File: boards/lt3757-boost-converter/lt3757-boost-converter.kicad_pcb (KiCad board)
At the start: 2 copper layers, 43.8 x 64.8 mm, 40 parts, among them J1 GND, J2 Enable, J3 BAT, J4 24V, J5 M3, J6 M3, J7 M3, J8 M3, J9 GND, Q1 FDB86566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

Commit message: [lt3757-boost-converter] add rev3 to silkscreen, set page properties
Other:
- board text added: "rev3"
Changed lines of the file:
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@@
     (links 69)
     (no_connects 1)
-    (area 46.914999 27.229999 90.880001 92.150001)
+    (area 46.355 22.13 92.184 94.175)
     (thickness 1.6)
-    (drawings 30)
+    (drawings 31)
     (tracks 120)
     (zones 0)
@@
     (nets 19)
   )
-  (page A4)
+  (page User 200 150.012)
+  (title_block
+    (title "24V Boost Converter")
+    (date 2017-06-19)
+    (rev rev3)
+    (company VIPER)
+  )
   (layers
     (0 F.Cu signal)
@@
       (net 2 GND))
   )
+  (gr_text rev3 (at 67.945 31.115 270) (layer F.SilkS)
+    (effects (font (size 1.5 1.5) (thickness 0.3)))
+  )
   (gr_line (start 46.99 34.29) (end 53.975 34.29) (layer F.SilkS) (width 0.2))

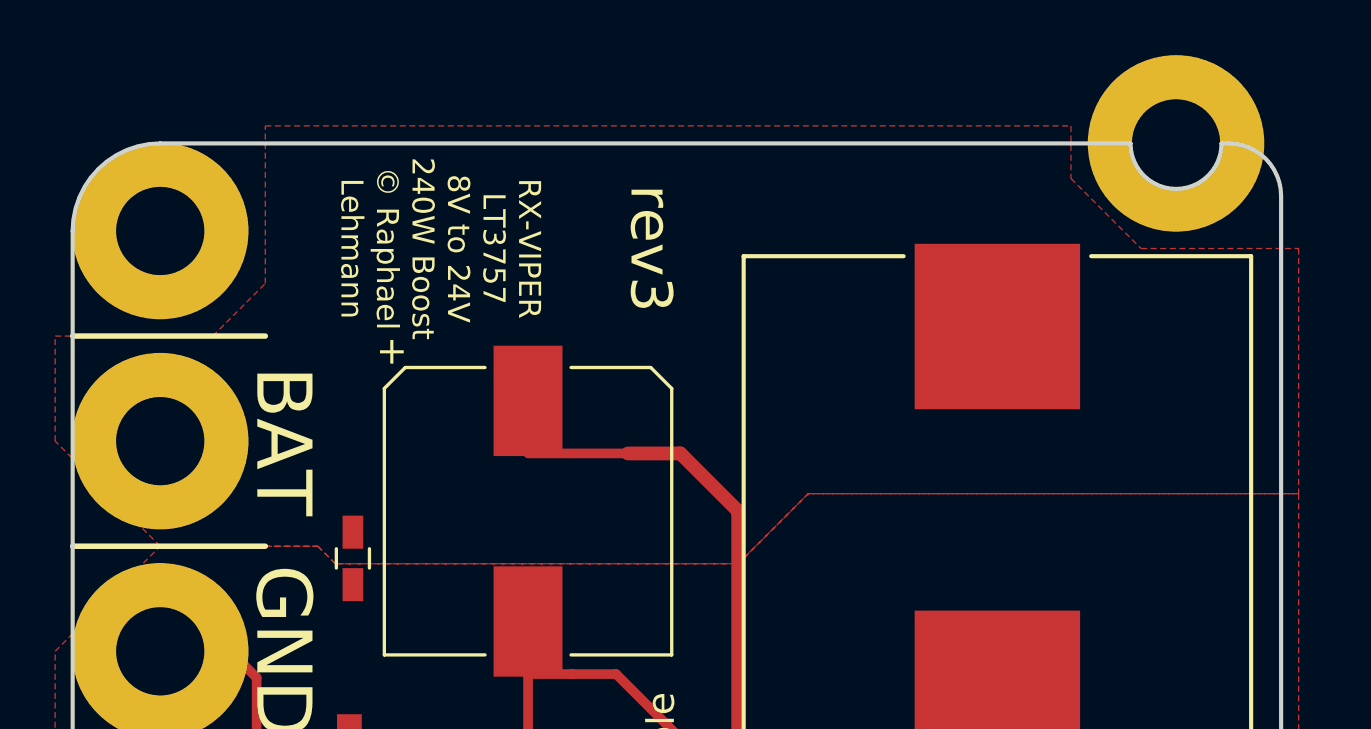
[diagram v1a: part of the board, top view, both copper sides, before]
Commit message: [lt3757-boost-converter] add label to cu layer
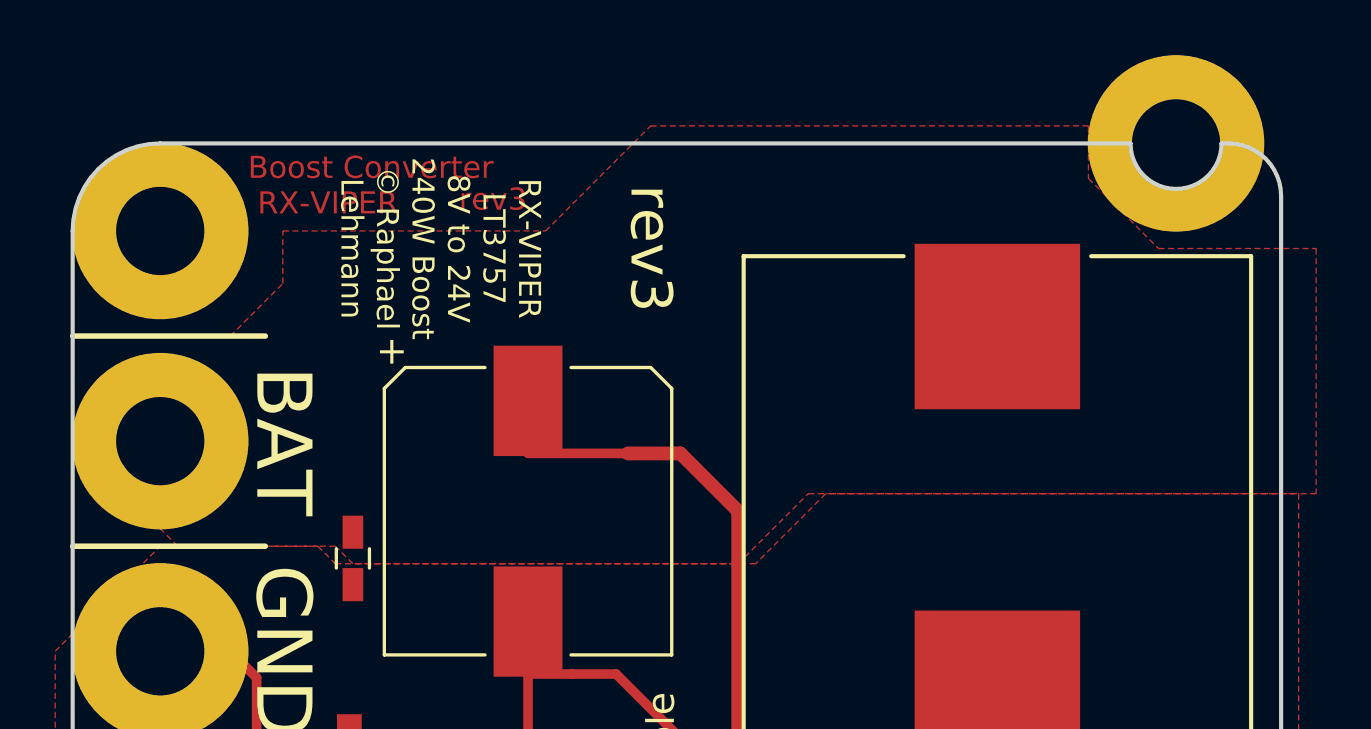
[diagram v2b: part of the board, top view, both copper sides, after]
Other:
- board text added: "Boost Converter RX-VIPER"
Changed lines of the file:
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@@
     (links 69)
     (no_connects 1)
-    (area 46.355 22.13 92.184 94.175)
+    (area 46.914999 27.229999 90.880001 92.150001)
     (thickness 1.6)
-    (drawings 31)
+    (drawings 33)
     (tracks 120)
     (zones 0)
@@
     (35 F.Paste user)
     (36 B.SilkS user)
-    (37 F.SilkS user)
+    (37 F.SilkS user hide)
     (38 B.Mask user)
     (39 F.Mask user)
@@
     (visible_elements FFFFFF7F)
     (pcbplotparams
-      (layerselection 0x00030_80000001)
-      (usegerberextensions false)
+      (layerselection 0x01080_00000001)
+      (usegerberextensions true)
       (excludeedgelayer true)
       (linewidth 0.100000)
       (plotframeref false)
-      (viasonmask false)
+      (viasonmask true)
       (mode 1)
       (useauxorigin false)
@@
       (outputformat 1)
       (mirror false)
-      (drillshape 1)
+      (drillshape 0)
       (scaleselection 1)
-      (outputdirectory ""))
+      (outputdirectory gerber/))
   )
   (net 0 "")
@@
     (pad 1 thru_hole circle (at 0 0) (size 6.4 6.4) (drill 3.2) (layers *.Cu *.Mask)
       (net 2 GND))
+  )
+  (gr_text rev3 (at 62.23 29.337) (layer F.Cu)
+    (effects (font (size 0.8 0.8) (thickness 0.15)))
+  )
+  (gr_text "Boost Converter\n RX-VIPER" (at 53.34 28.829) (layer F.Cu)
+    (effects (font (size 0.8 0.8) (thickness 0.15)) (justify left))
   )
   (gr_text rev3 (at 67.945 31.115 270) (layer F.SilkS)
@@
     (polygon
       (pts
-        (xy 53.975 32.385) (xy 53.975 26.67) (xy 83.185 26.67) (xy 83.185 28.575) (xy 85.725 31.115)
-        (xy 91.44 31.115) (xy 91.44 40.005) (xy 73.66 40.005) (xy 71.12 42.545) (xy 56.515 42.545)
-        (xy 55.88 41.91) (xy 50.165 41.91) (xy 46.355 38.1) (xy 46.355 34.29) (xy 52.07 34.29)
+        (xy 54.61 32.385) (xy 54.61 30.48) (xy 61.595 30.48) (xy 64.135 30.48) (xy 67.945 26.67)
+        (xy 83.82 26.67) (xy 83.82 28.575) (xy 86.36 31.115) (xy 92.075 31.115) (xy 92.075 40.005)
+        (xy 74.295 40.005) (xy 71.755 42.545) (xy 57.15 42.545) (xy 56.515 41.91) (xy 50.8 41.91)
+        (xy 46.99 38.1) (xy 46.99 34.29) (xy 52.705 34.29)
       )
     )

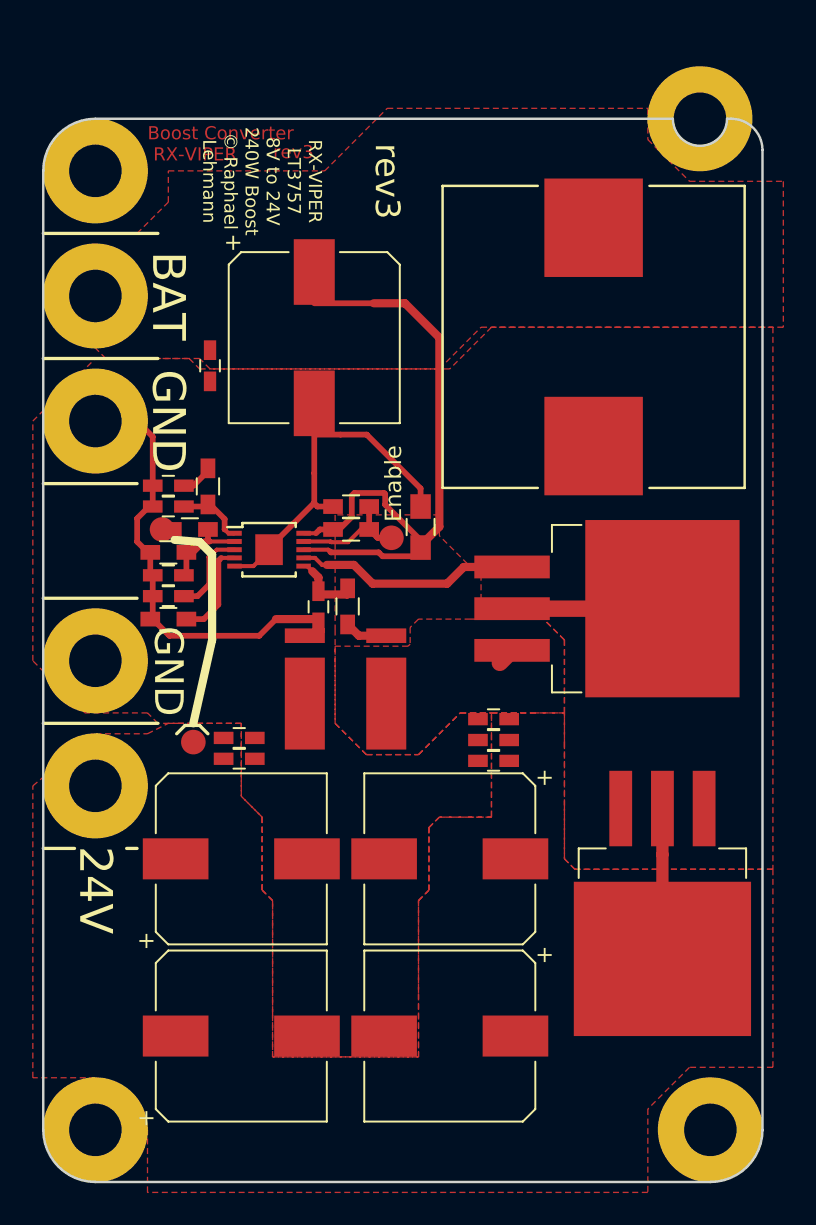
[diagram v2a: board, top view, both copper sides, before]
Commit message: [lt3757-boost-converter] adjust to LeitOn design rules
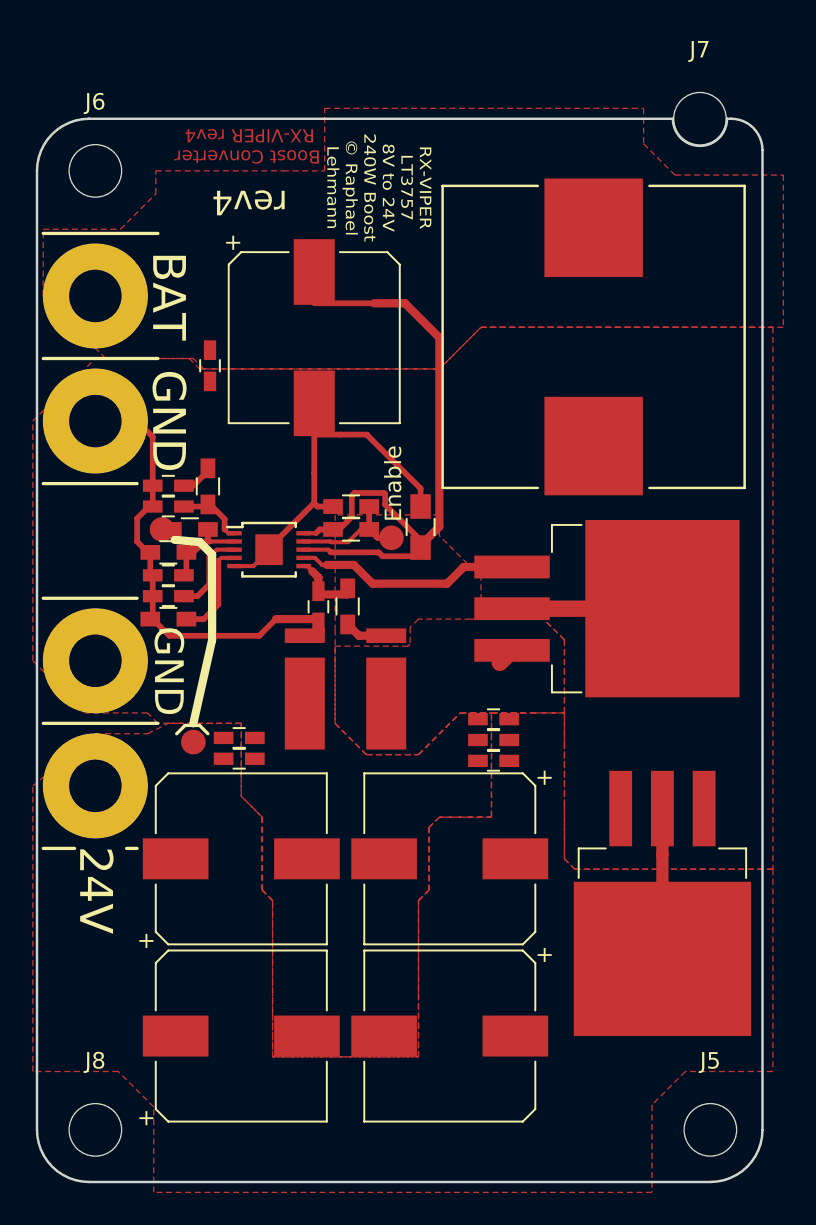
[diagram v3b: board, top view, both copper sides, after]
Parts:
- C12: value 1µ -> 10µ
- C13, C14: value 100n -> 1µ
- C15: value 47n -> 100n
- C16: value 10n -> 100n
- J5, J6, J7, J8: footprint Mounting_Holes:MountingHole_3.2mm_M3_Pad -> Mounting_Holes:MountingHole_3.2mm_M3
- U1: footprint Housings_SSOP:MSOP-10-1EP_3x3mm_Pitch0.5mm -> MSOP-10-1EP_3x3mm_Pitch0.5mm:MSOP-10-1EP_3x3mm_Pitch0.5mm
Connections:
- J5 pad 1: Net-(J5-Pad1) -> (no net)
- J6 pad 1: Net-(J6-Pad1) -> (no net)
- J7 pad 1: Net-(J7-Pad1) -> (no net)
- J8 pad 1: Net-(J8-Pad1) -> (no net)
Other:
- board size 43.8 x 64.8 mm -> 44.2 x 64.8 mm
- board text added: "Boost Converter RX-VIPER rev4"
- board text added: "rev4"
- board text removed: "Boost Converter RX-VIPER"
- board text removed: "rev3"
